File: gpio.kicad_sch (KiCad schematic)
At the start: 4 parts, among them J3 Pyro Connectors

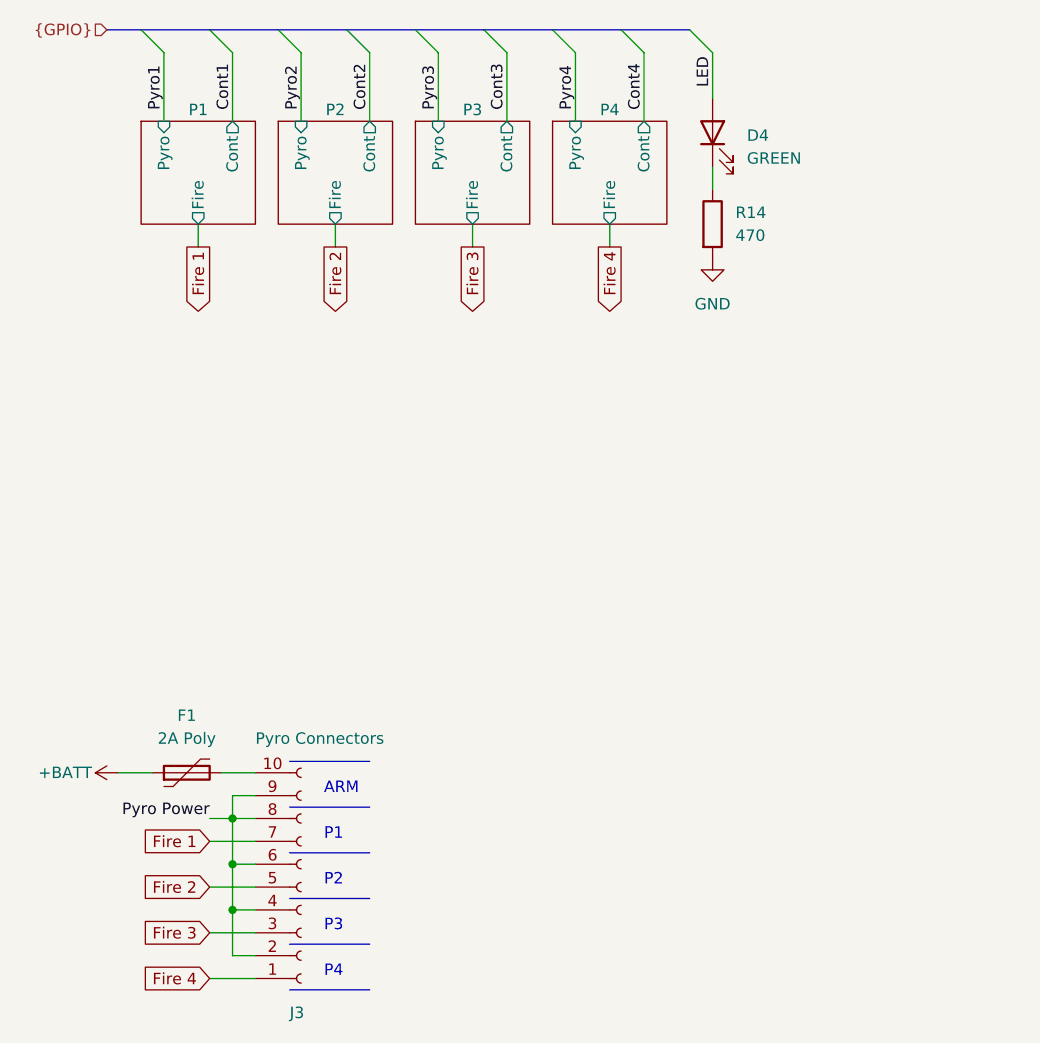
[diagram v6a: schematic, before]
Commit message: Geographical reannotated
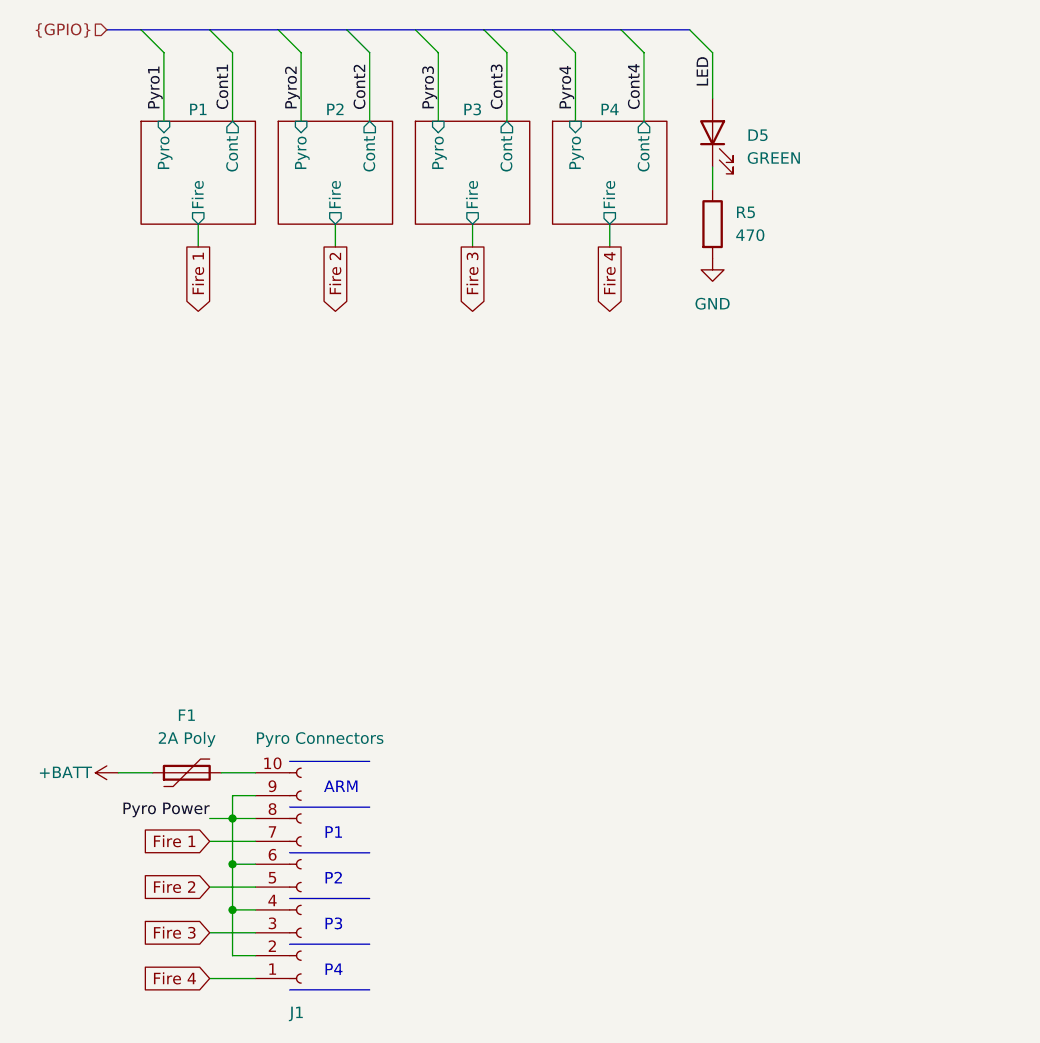
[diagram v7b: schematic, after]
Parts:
- renumbered D4 to D5, J3 to J1, R14 to R5
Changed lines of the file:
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@@
   (symbol (lib_id "Connector:Conn_01x10_Female") (at 45.72 116.84 0) (mirror x) (unit 1)
     (in_bom yes) (on_board yes)
-    (property "Reference" "J3" (id 0) (at 44.45 130.81 0)
+    (property "Reference" "J1" (id 0) (at 44.45 130.81 0)
       (effects (font (size 1.27 1.27)) (justify left))
     )
@@
   (symbol (lib_id "Device:R") (at 91.44 43.18 0) (unit 1)
     (in_bom yes) (on_board yes) (fields_autoplaced)
-    (property "Reference" "R14" (id 0) (at 93.98 41.9099 0)
+    (property "Reference" "R5" (id 0) (at 93.98 41.9099 0)
       (effects (font (size 1.27 1.27)) (justify left))
     )
@@
   (symbol (lib_id "Device:LED") (at 91.44 33.02 90) (unit 1)
     (in_bom yes) (on_board yes) (fields_autoplaced)
-    (property "Reference" "D4" (id 0) (at 95.25 33.3374 90)
+    (property "Reference" "D5" (id 0) (at 95.25 33.3374 90)
       (effects (font (size 1.27 1.27)) (justify right))
     )

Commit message: Final refinements before issue to JLC
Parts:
- renumbered D5 to D4, J1 to J4, R5 to R14
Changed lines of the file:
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@@
   (symbol (lib_id "Connector:Conn_01x10_Female") (at 45.72 116.84 0) (mirror x) (unit 1)
     (in_bom yes) (on_board yes)
-    (property "Reference" "J1" (id 0) (at 44.45 130.81 0)
+    (property "Reference" "J4" (id 0) (at 44.45 130.81 0)
       (effects (font (size 1.27 1.27)) (justify left))
     )
@@
   (symbol (lib_id "Device:R") (at 91.44 43.18 0) (unit 1)
     (in_bom yes) (on_board yes) (fields_autoplaced)
-    (property "Reference" "R5" (id 0) (at 93.98 41.9099 0)
+    (property "Reference" "R14" (id 0) (at 93.98 41.9099 0)
       (effects (font (size 1.27 1.27)) (justify left))
     )
@@
   (symbol (lib_id "power:GND") (at 91.44 46.99 0) (unit 1)
     (in_bom yes) (on_board yes) (fields_autoplaced)
-    (property "Reference" "#PWR068" (id 0) (at 91.44 53.34 0)
+    (property "Reference" "#PWR070" (id 0) (at 91.44 53.34 0)
       (effects (font (size 1.27 1.27)) hide)
     )
@@
   (symbol (lib_id "Device:LED") (at 91.44 33.02 90) (unit 1)
     (in_bom yes) (on_board yes) (fields_autoplaced)
-    (property "Reference" "D5" (id 0) (at 95.25 33.3374 90)
+    (property "Reference" "D4" (id 0) (at 95.25 33.3374 90)
       (effects (font (size 1.27 1.27)) (justify right))
     )
@@
   (symbol (lib_id "power:+BATT") (at 25.4 104.14 90) (unit 1)
     (in_bom yes) (on_board yes)
-    (property "Reference" "#PWR067" (id 0) (at 29.21 104.14 0)
+    (property "Reference" "#PWR069" (id 0) (at 29.21 104.14 0)
       (effects (font (size 1.27 1.27)) hide)
     )
